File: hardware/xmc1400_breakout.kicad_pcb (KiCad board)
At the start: 2 copper layers, 50 x 40 mm, 31 parts, among them P1 CON-SENSOR2, P2 BOOT, P3 CONN_01X12, P4 CONN_01X12, P5 CONN_01X12, P6 CONN_01X12, U1 XMC1XXX48, U2 DRILL, U3 DRILL, U4 DRILL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

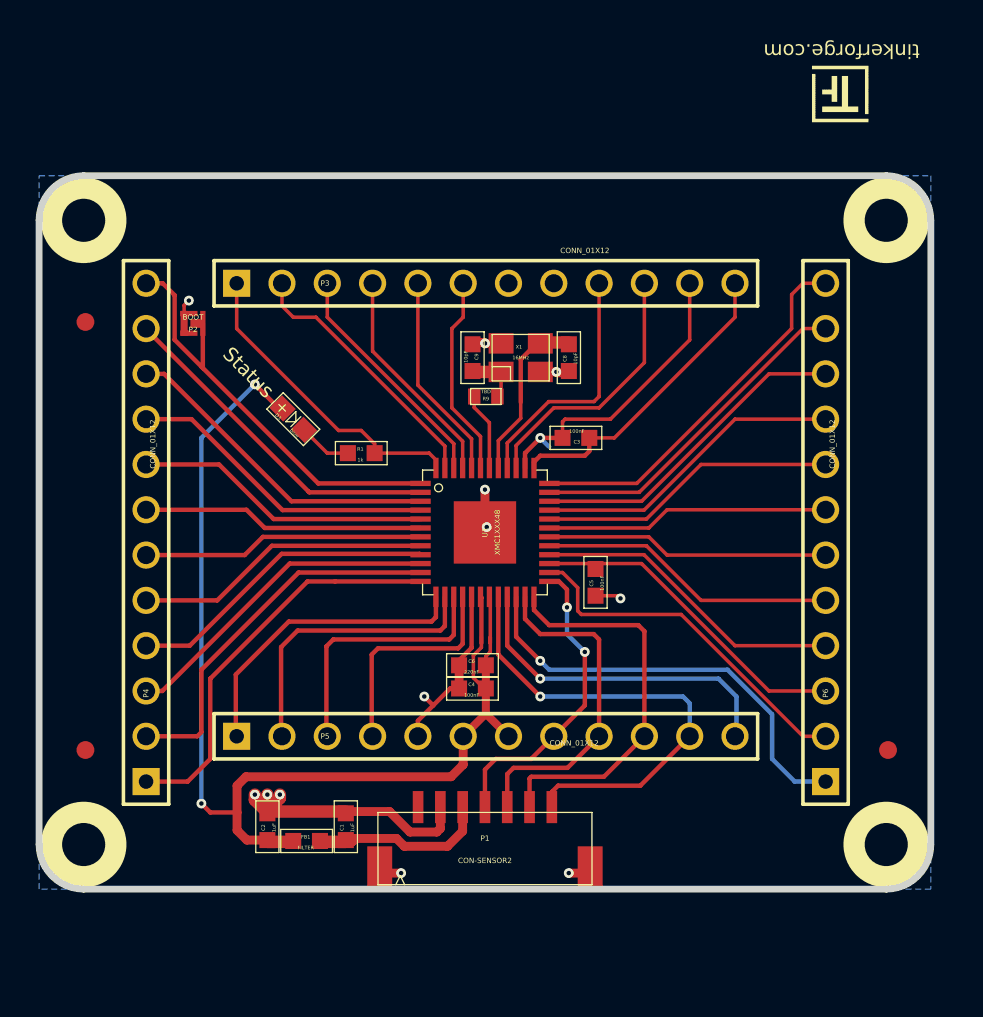
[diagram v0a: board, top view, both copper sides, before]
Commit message: Add VCC connections
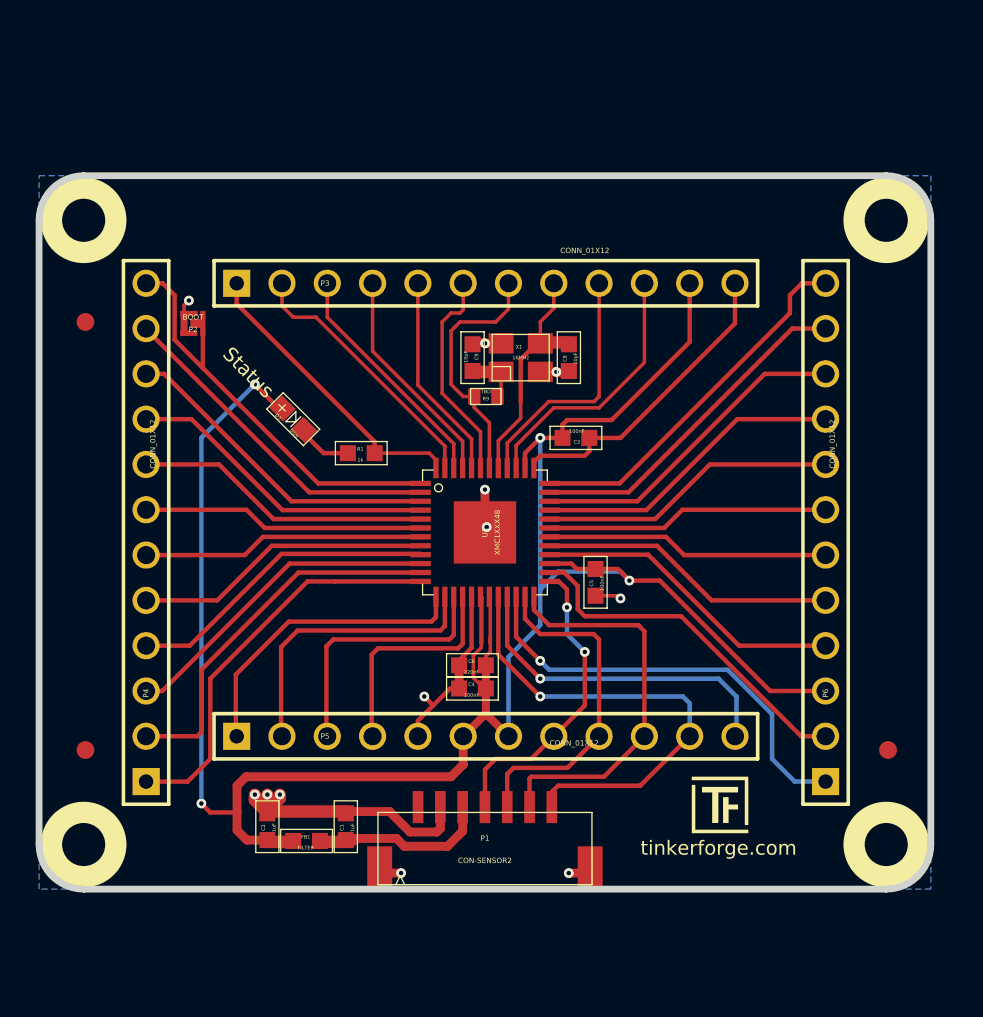
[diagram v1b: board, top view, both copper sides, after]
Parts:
- moved G*** 38.0 mm to (156.9, 116.8), turned to 0 degrees
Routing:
- net VCC: track 102.5 -> 125.3 mm, vias 3 -> 4
- net Pin42: track 4.36 -> 14.1 mm
- net Pin41: track 9.70 -> 13.4 mm
- net Pin43: track 11.3 -> 12.0 mm
- net Pin48: track 17.5 -> 16.8 mm
- net Pin36: track 21.3 -> 20.7 mm

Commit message: Add pin markings
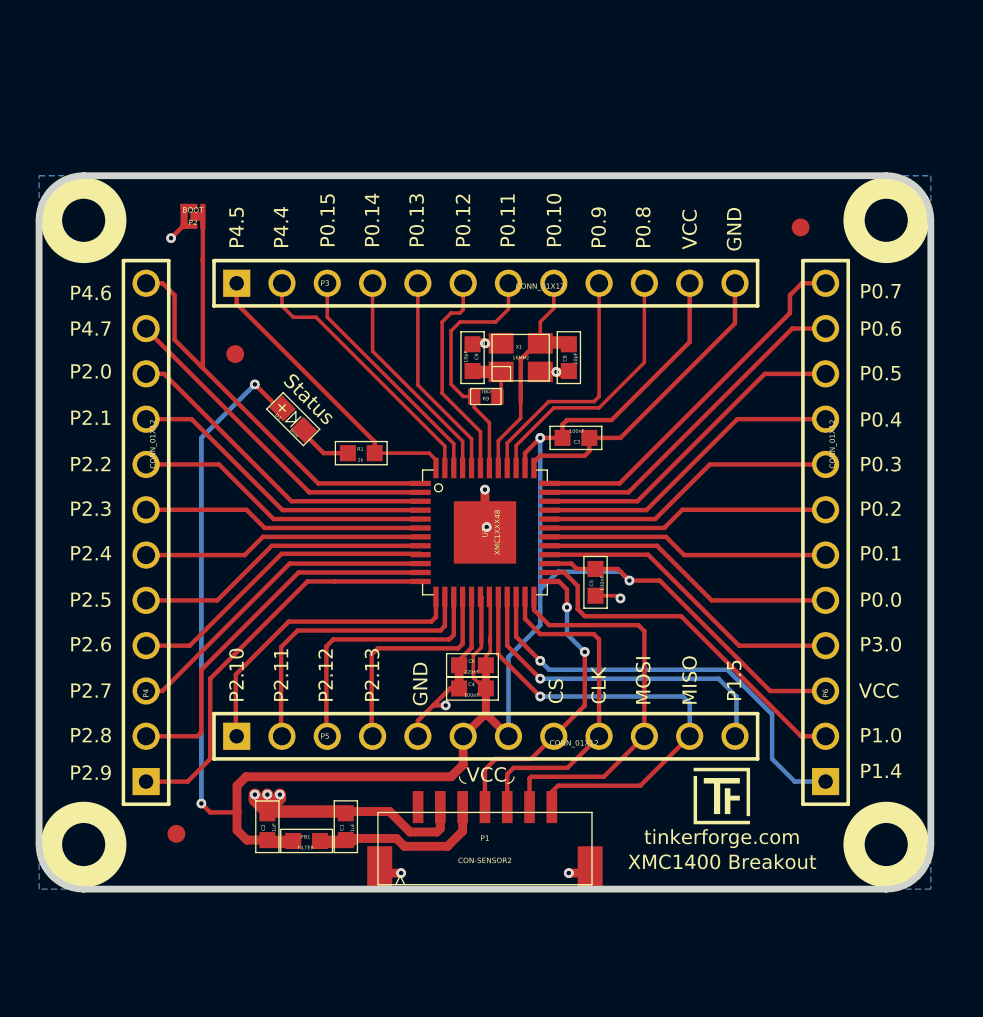
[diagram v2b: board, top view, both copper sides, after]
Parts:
- moved Fiducial_Mark 29.7 mm to (163.0, 86.0)
- moved Fiducial_Mark 8.59 mm to (131.3, 93.1)
- moved Fiducial_Mark 6.94 mm to (128.0, 120.0)
- moved P2 6.00 mm to (128.9, 85.4)
- moved G*** 0.51 mm to (157.0, 116.3)
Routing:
- net Pin1: track 24.5 -> 30.6 mm
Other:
- board text added: "CLK"
- board text added: "CS"
- board text added: "GND"
- board text added: "MISO"
- board text added: "MOSI"
- board text added: "P0.0"
- board text added: "P0.1"
- board text added: "P0.10"
- board text added: "P0.11"
- board text added: "P0.12"
- board text added: "P0.13"
- board text added: "P0.14"
- board text added: "P0.15"
- board text added: "P0.2"
- board text added: "P0.3"
- board text added: "P0.4"
- board text added: "P0.5"
- board text added: "P0.6"
- board text added: "P0.7"
- board text added: "P0.8"
- board text added: "P0.9"
- board text added: "P1.0"
- board text added: "P1.4"
- board text added: "P1.5"
- board text added: "P2.0"
- board text added: "P2.1"
- board text added: "P2.10"
- board text added: "P2.11"
- board text added: "P2.12"
- board text added: "P2.13"
- board text added: "P2.2"
- board text added: "P2.3"
- board text added: "P2.4"
- board text added: "P2.5"
- board text added: "P2.6"
- board text added: "P2.7"
- board text added: "P2.8"
- board text added: "P2.9"
- board text added: "P3.0"
- board text added: "P4.4"
- board text added: "P4.5"
- board text added: "P4.6"
- board text added: "P4.7"
- board text added: "VCC"
- board text added: "XMC1400 Breakout"
- board text added: "◟VCC◞"

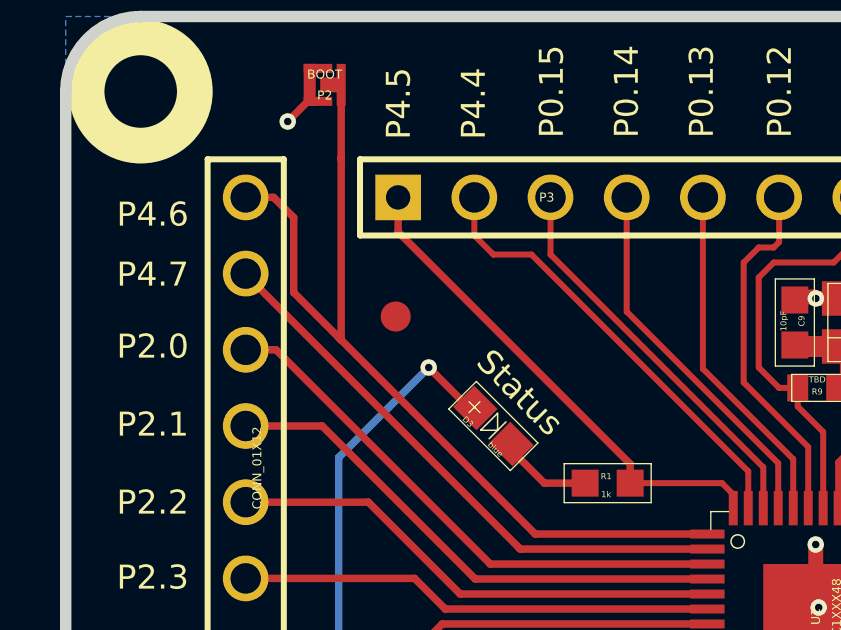
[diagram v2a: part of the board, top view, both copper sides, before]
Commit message: Fix fiducial mark position top left
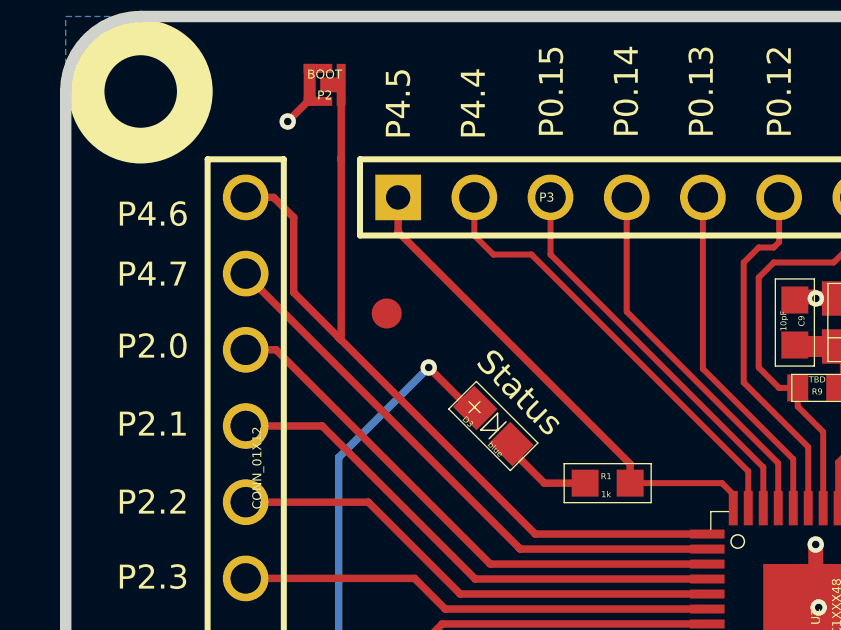
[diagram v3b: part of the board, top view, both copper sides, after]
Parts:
- moved Fiducial_Mark 0.32 mm to (131.0, 93.0)
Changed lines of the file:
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@@
   )
   (module kicad-libraries:Fiducial_Mark (layer Vorderseite)
-    (at 131.3 93.1)
+    (at 131 93)
     (attr smd)
     (fp_text reference Fiducial_Mark (at 0 0) (layer F.SilkS) hide

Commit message: delete bottom silkscreen stuff
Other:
- board text removed: "1"
- board text removed: "2"
- board text removed: "3"
- board text removed: "4"
- board text removed: "Full-Duplex Non-Terminated"
- board text removed: "Full-Duplex Terminated"
- board text removed: "Half-Duplex Non-Terminated"
- board text removed: "Half-Duplex Terminated"
- board text removed: "ON"

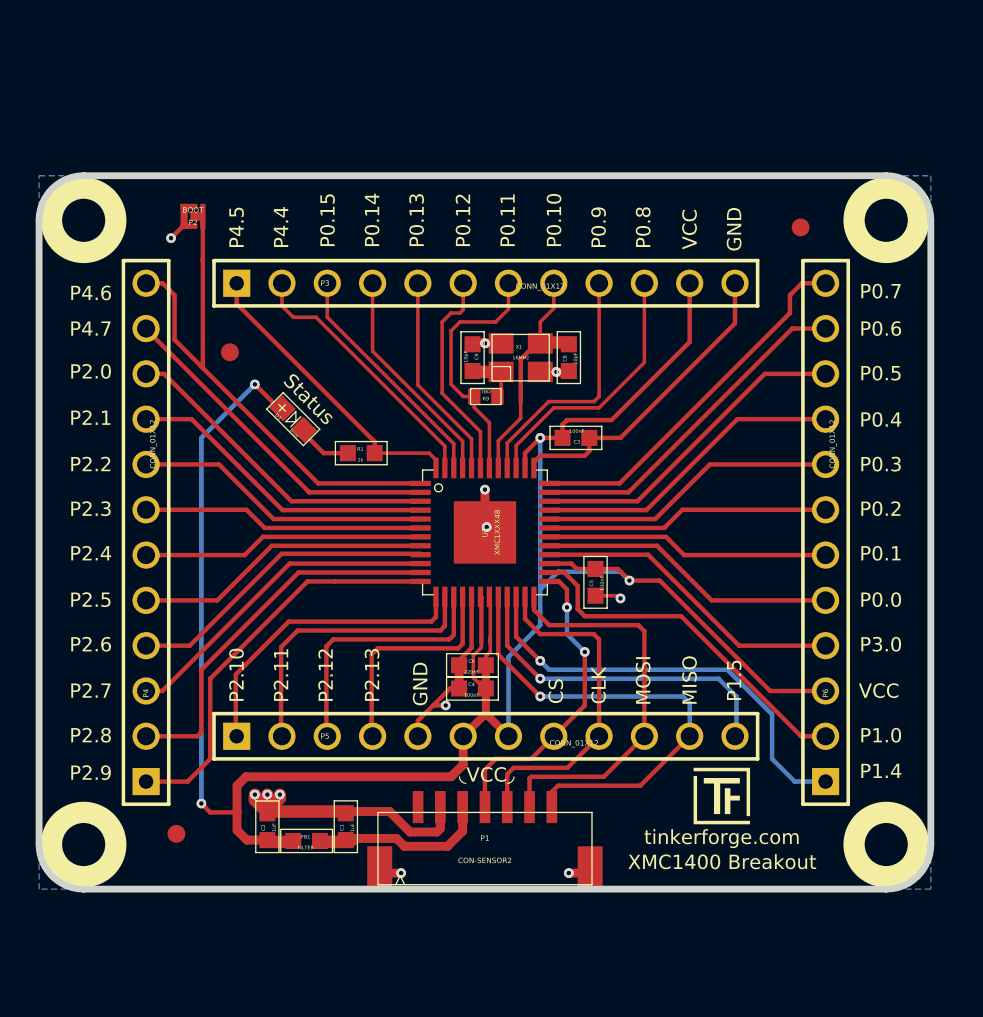
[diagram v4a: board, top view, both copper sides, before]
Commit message: Add 3d information
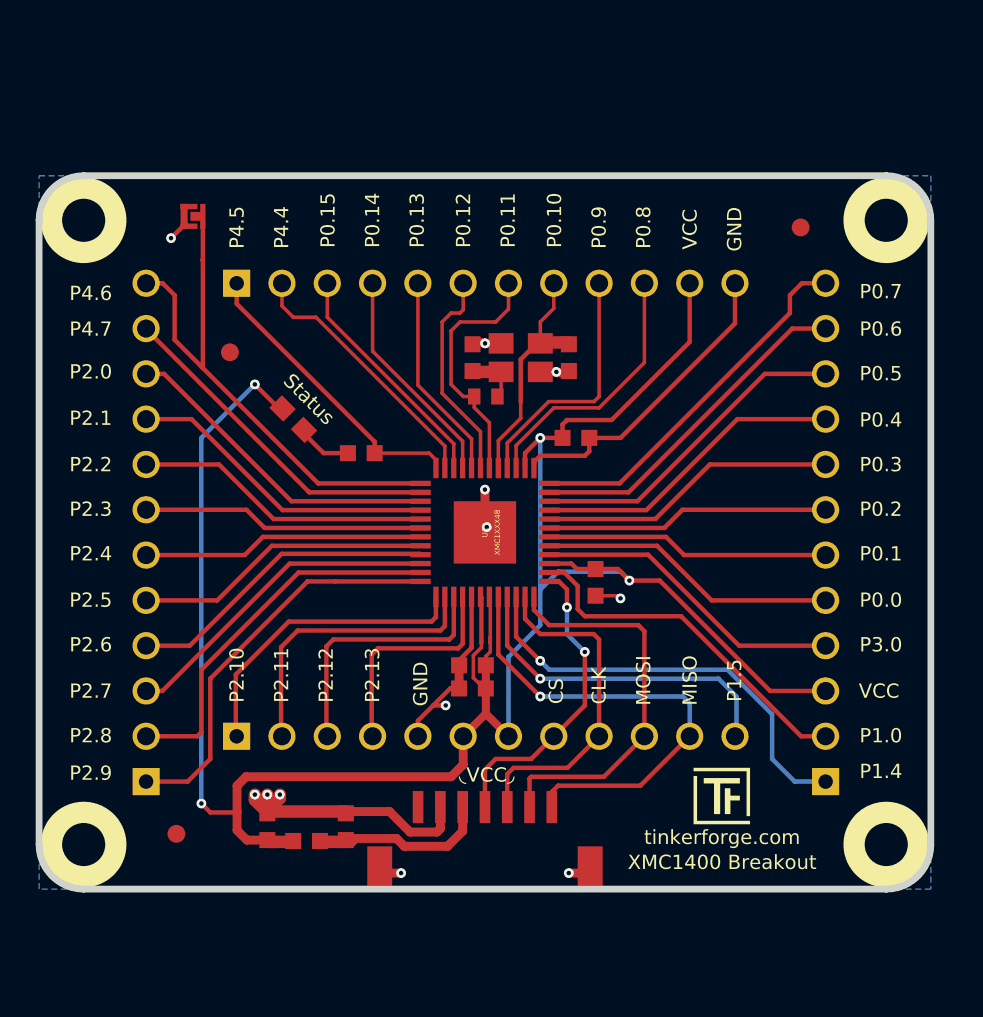
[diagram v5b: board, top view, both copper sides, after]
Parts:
- C1, C2, C3, C4, C5, C6, C8, C9, FB1: footprint 0603F -> C0603F
- R1: footprint 0603F -> R0603F
- R9: footprint 0402E -> R0402E

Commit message: Add more headers (GND, VCC, 5V)
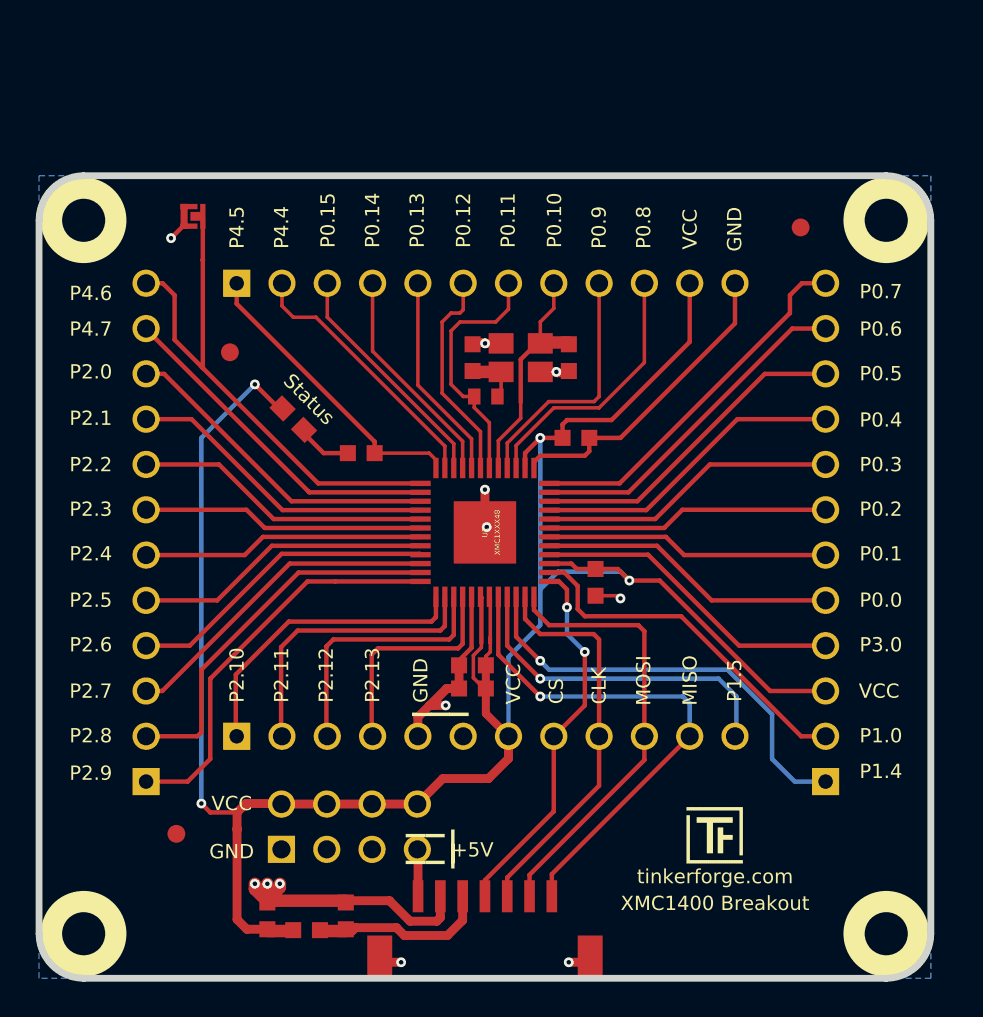
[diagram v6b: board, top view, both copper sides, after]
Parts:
- added P7: CONN_02X04, kicad-libraries:pin_array_4x2, F.Cu at (137.7, 119.6)
- moved G*** 22.5 mm to (135.7, 110.1)
- moved VAL 22.5 mm to (135.7, 95.1)
- moved VAL 22.4 mm to (135.7, 103.3)
- moved C1 5.00 mm to (137.5, 124.6)
- moved C2 5.00 mm to (133.1, 124.6)
- moved FB1 5.00 mm to (135.3, 125.4)
- moved P1 5.00 mm to (145.3, 128.1)
- moved U3 5.00 mm to (122.8, 125.6)
- moved U4 5.00 mm to (167.8, 125.6)
- moved G*** 2.24 mm to (156.6, 118.5)
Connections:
- P1 pad 1: Net-(P1-Pad1) -> +5V
- P5 pad 6: VCC -> GND
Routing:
- net VCC: track 125.3 -> 129.5 mm
- net S-CS: track 17.8 -> 21.6 mm
- net S-CLK: track 19.2 -> 22.4 mm
- net GND: track 55.5 -> 58.6 mm
- net +5V: track 0.00 -> 2.65 mm
- net S-MOSI: track 22.3 -> 24.9 mm
- net S-MISO: track 26.8 -> 29.1 mm
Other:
- board size 50 x 40 mm -> 50 x 45 mm
- board text added: "+5V"
- board text added: "_"
- board text added: "___"
- board text removed: "◟VCC◞"

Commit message: Fix typo
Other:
- board text added: "status"
- board text removed: "Status"
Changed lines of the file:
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@@
     (links 99)
     (no_connects 1)
-    (area 120.109499 82.909499 170.490501 128.290501)
+    (area 119.445139 82.245139 282.895869 162.490743)
     (thickness 1.6002)
     (drawings 70)
@@
   (layers
     (0 Vorderseite signal)
-    (31 Rückseite signal)
+    (31 Rückseite signal hide)
     (32 B.Adhes user)
     (33 F.Adhes user)
@@
   )
   (setup
-    (last_trace_width 0.5)
+    (last_trace_width 0.2)
     (user_trace_width 0.25)
     (user_trace_width 0.29972)
@@
   (gr_line (start 122.8 83.1) (end 167.8 83.1) (angle 90) (layer Edge.Cuts) (width 0.381))
   (gr_arc (start 167.8 125.6) (end 170.3 125.6) (angle 90) (layer Edge.Cuts) (width 0.381))
-  (gr_text Status (at 134.2 94.4 315) (layer F.SilkS)
+  (gr_text status (at 134.2 94.4 315) (layer F.SilkS)
     (effects (font (size 0.8 0.8) (thickness 0.15)) (justify left))
   )

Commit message: Fix conductor path connection
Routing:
- net VCC: track 129.5 -> 132.0 mm
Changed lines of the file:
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@@
   (general
     (links 99)
-    (no_connects 1)
-    (area 119.445139 82.245139 282.895869 162.490743)
+    (no_connects 0)
+    (area 120.109499 82.909499 170.490501 128.290501)
     (thickness 1.6002)
     (drawings 70)
-    (tracks 377)
+    (tracks 378)
     (zones 0)
     (modules 32)
@@
   (via (at 145.305 92.5) (size 0.55) (drill 0.25) (layers Vorderseite Rückseite) (net 1))
   (segment (start 145.2549 92.4499) (end 145.305 92.5) (width 0.5) (layer Vorderseite) (net 1))
+  (segment (start 136.43 118.33) (end 133.89 118.33) (width 0.2) (layer Vorderseite) (net 2))
   (segment (start 131.4 118.8) (end 131.9 118.3) (width 0.5) (layer Vorderseite) (net 2))
   (segment (start 131.9 118.3) (end 133.86 118.3) (width 0.5) (layer Vorderseite) (net 2))
